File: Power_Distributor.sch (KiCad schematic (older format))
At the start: 0 parts

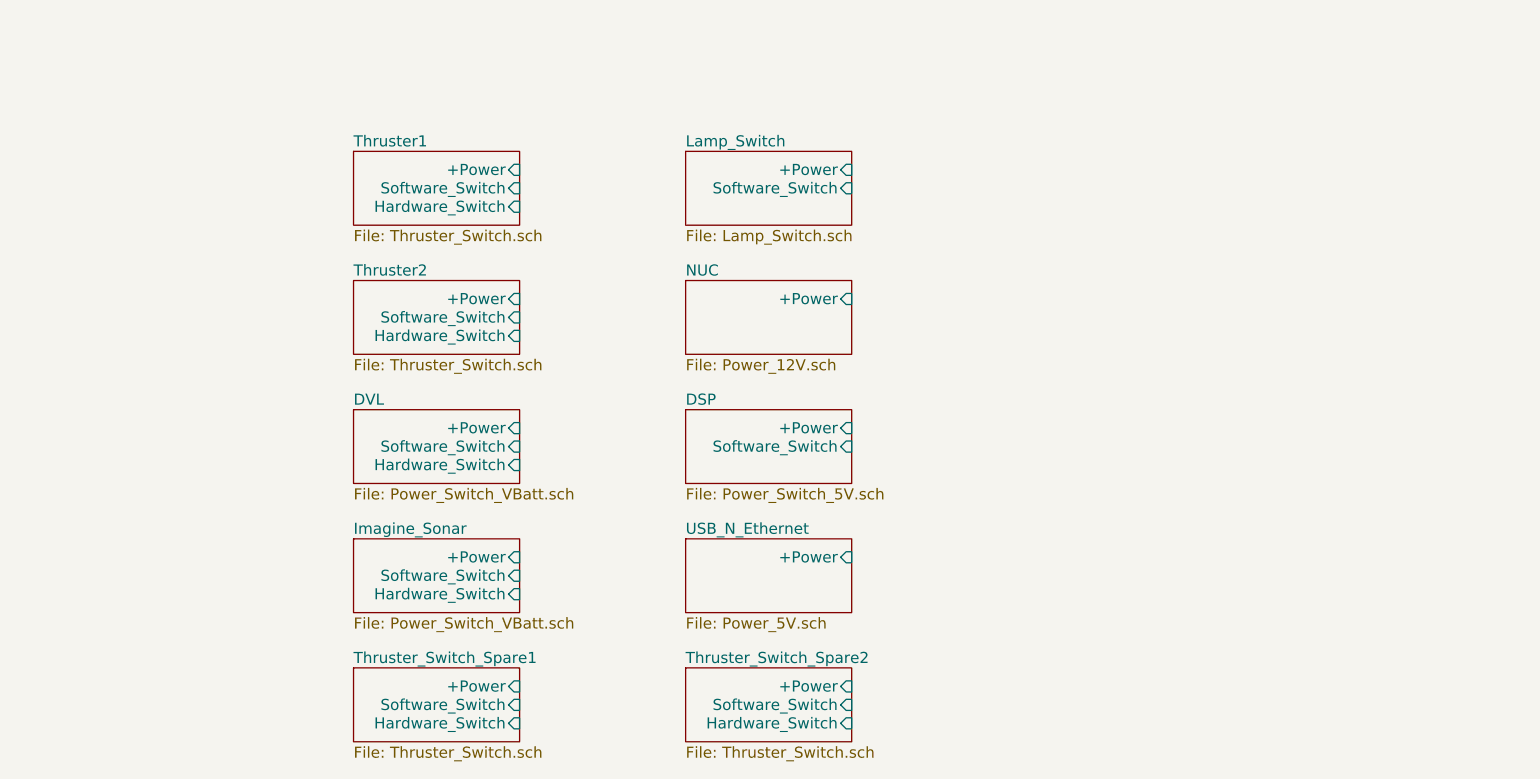
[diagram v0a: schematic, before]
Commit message: import Power-Controller.sch, add Thruster_Off_Switch and add VBatt
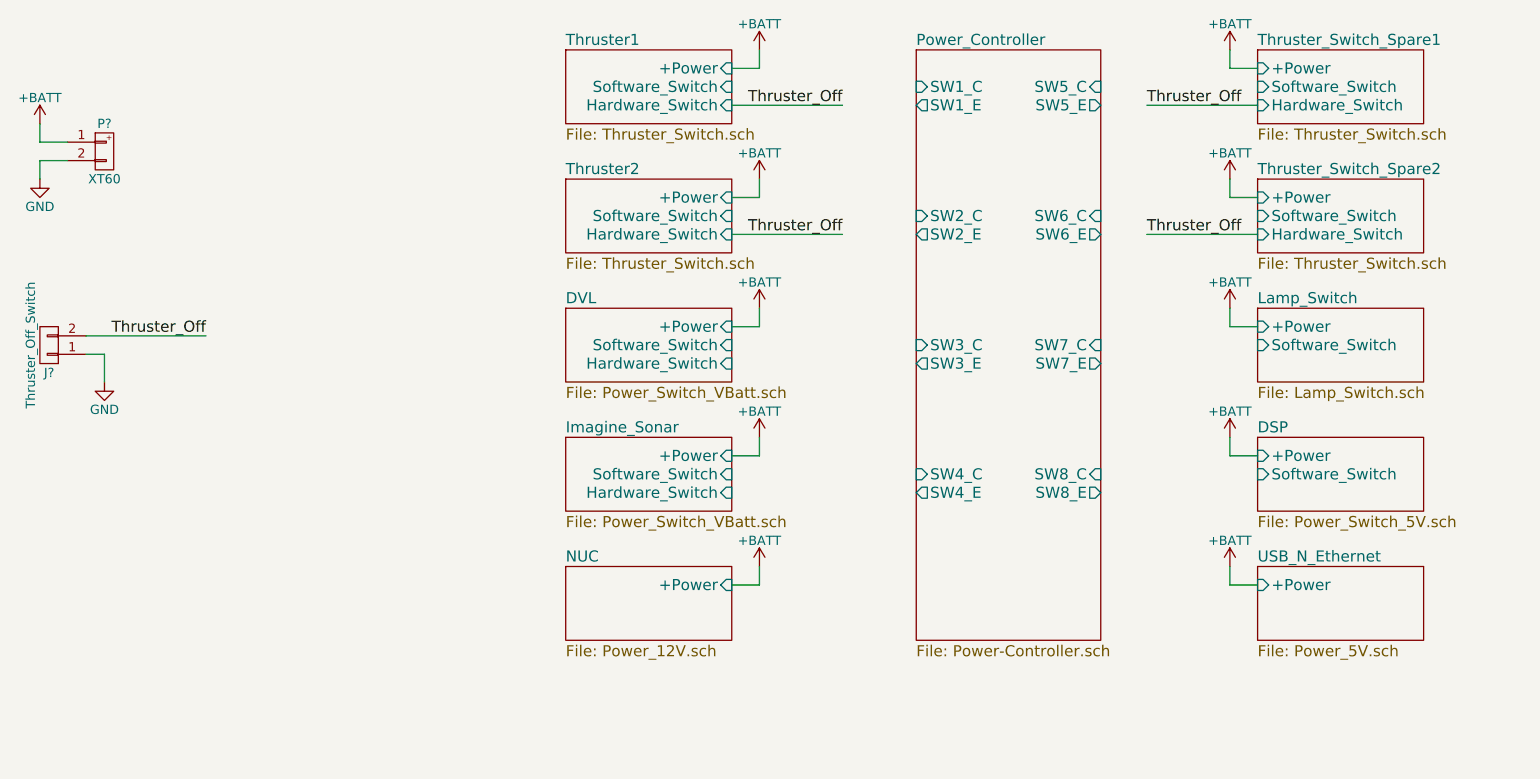
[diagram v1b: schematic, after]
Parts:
- added J?: Thruster_Off_Switch, symbol CONN_01X02
- added P?: XT60, symbol XT60
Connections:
- new net +BATT: P?.1 (P1)
- new net GND: J?.1 (P1), P?.2 (P2)
- new net Thruster_Off: J?.2 (P2)
